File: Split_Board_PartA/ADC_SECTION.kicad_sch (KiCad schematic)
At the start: 58 parts, among them J2 Conn_01x28, U26 MCP604, U27 MCP604, U28 ADC128S102CIMTX_NOPB

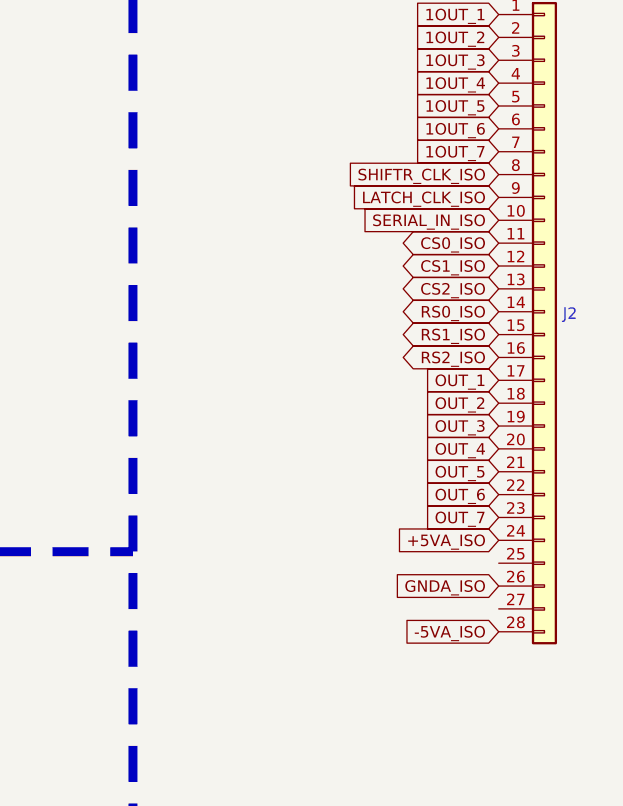
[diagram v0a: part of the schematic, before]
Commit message: added led pins in part A of slave boards
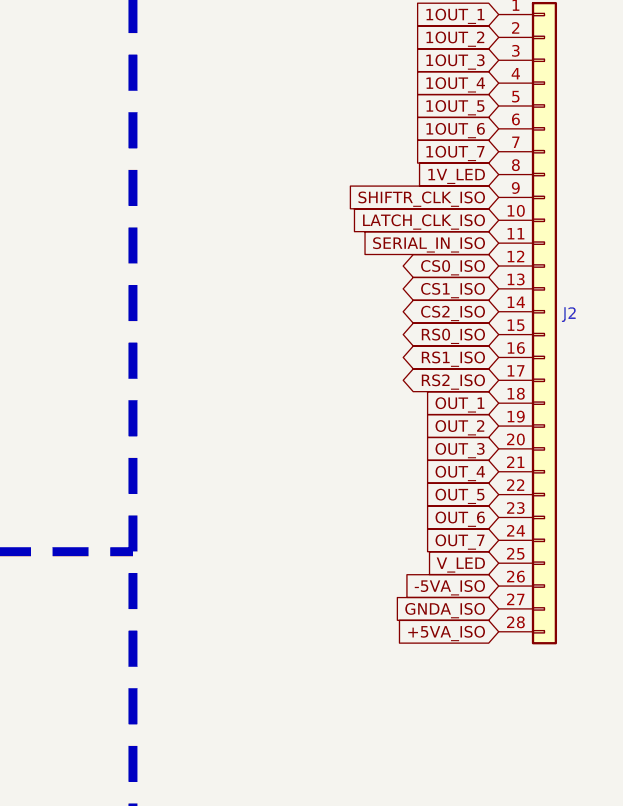
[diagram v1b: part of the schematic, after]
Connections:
- net +5VA_ISO: now also J2.28 (Pin_28); no longer J2.24 (Pin_24)
- net -5VA_ISO: now also J2.26 (Pin_26); no longer J2.28 (Pin_28)
- net CS0_ISO: now also J2.12 (Pin_12); no longer J2.11 (Pin_11)
- net CS1_ISO: now also J2.13 (Pin_13); no longer J2.12 (Pin_12)
- net CS2_ISO: now also J2.14 (Pin_14); no longer J2.13 (Pin_13)
- net GNDA_ISO: now also J2.27 (Pin_27); no longer J2.26 (Pin_26)
- net LATCH_CLK_ISO: now also J2.10 (Pin_10); no longer J2.9 (Pin_9)
- net OUT_1: now also J2.18 (Pin_18); no longer J2.17 (Pin_17)
- net OUT_2: now also J2.19 (Pin_19); no longer J2.18 (Pin_18)
- net OUT_3: now also J2.20 (Pin_20); no longer J2.19 (Pin_19)
- net OUT_4: now also J2.21 (Pin_21); no longer J2.20 (Pin_20)
- net OUT_5: now also J2.22 (Pin_22); no longer J2.21 (Pin_21)
- net OUT_6: now also J2.23 (Pin_23); no longer J2.22 (Pin_22)
- net OUT_7: now also J2.24 (Pin_24); no longer J2.23 (Pin_23)
- net RS0_ISO: now also J2.15 (Pin_15); no longer J2.14 (Pin_14)
- net RS1_ISO: now also J2.16 (Pin_16); no longer J2.15 (Pin_15)
- net RS2_ISO: now also J2.17 (Pin_17); no longer J2.16 (Pin_16)
- net SERIAL_IN_ISO: now also J2.11 (Pin_11); no longer J2.10 (Pin_10)
- net SHIFTR_CLK_ISO: now also J2.9 (Pin_9); no longer J2.8 (Pin_8)
- net V_LED: now reaches J2.25 (Pin_25)
- new net 1V_LED: J2.8 (Pin_8)

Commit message: Removed the gerber files of espv5.0
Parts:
- R61, R62, R63, R64, R67, R68, R71, R72: value 100E -> 0E
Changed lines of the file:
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@@
       (effects (font (size 1.27 1.27)) (justify right))
     )
-    (property "Value" "100E" (at 100.457 60.1472 0)
+    (property "Value" "0E" (at 100.457 60.1472 0)
       (effects (font (size 1.27 1.27)) (justify right))
     )
@@
       (effects (font (size 1.27 1.27)) (justify right))
     )
-    (property "Value" "100E" (at 49.657 190.3222 0)
+    (property "Value" "0E" (at 49.657 190.3222 0)
       (effects (font (size 1.27 1.27)) (justify right))
     )
@@
       (effects (font (size 1.27 1.27)) (justify right))
     )
-    (property "Value" "100E" (at 100.457 190.3222 0)
+    (property "Value" "0E" (at 100.457 190.3222 0)
       (effects (font (size 1.27 1.27)) (justify right))
     )
@@
       (effects (font (size 1.27 1.27)) (justify right))
     )
-    (property "Value" "100E" (at 49.657 215.7222 0)
+    (property "Value" "0E" (at 49.657 215.7222 0)
       (effects (font (size 1.27 1.27)) (justify right))
     )
@@
       (effects (font (size 1.27 1.27)) (justify right))
     )
-    (property "Value" "100E" (at 49.657 85.5472 0)
+    (property "Value" "0E" (at 49.657 85.5472 0)
       (effects (font (size 1.27 1.27)) (justify right))
     )
@@
       (effects (font (size 1.27 1.27)) (justify right))
     )
-    (property "Value" "100E" (at 100.457 85.5472 0)
+    (property "Value" "0E" (at 100.457 85.5472 0)
       (effects (font (size 1.27 1.27)) (justify right))
     )
@@
       (effects (font (size 1.27 1.27)) (justify right))
     )
-    (property "Value" "100E" (at 50.292 110.9472 0)
+    (property "Value" "0E" (at 50.292 110.9472 0)
       (effects (font (size 1.27 1.27)) (justify right))
     )
@@
       (effects (font (size 1.27 1.27)) (justify right))
     )
-    (property "Value" "100E" (at 100.457 241.1222 0)
+    (property "Value" "0E" (at 100.457 241.1222 0)
       (effects (font (size 1.27 1.27)) (justify right))
     )
@@
       (effects (font (size 1.27 1.27)) (justify right))
     )
-    (property "Value" "100E" (at 49.657 60.1472 0)
+    (property "Value" "0E" (at 49.657 60.1472 0)
       (effects (font (size 1.27 1.27)) (justify right))
     )
@@
       (effects (font (size 1.27 1.27)) (justify right))
     )
-    (property "Value" "100E" (at 100.457 110.9472 0)
+    (property "Value" "0E" (at 100.457 110.9472 0)
       (effects (font (size 1.27 1.27)) (justify right))
     )
@@
       (effects (font (size 1.27 1.27)) (justify right))
     )
-    (property "Value" "100E" (at 101.092 168.0972 0)
+    (property "Value" "0E" (at 101.092 168.0972 0)
       (effects (font (size 1.27 1.27)) (justify right))
     )
@@
       (effects (font (size 1.27 1.27)) (justify right))
     )
-    (property "Value" "100E" (at 47.752 37.9222 0)
+    (property "Value" "0E" (at 47.752 37.9222 0)
       (effects (font (size 1.27 1.27)) (justify right))
     )
@@
       (effects (font (size 1.27 1.27)) (justify right))
     )
-    (property "Value" "100E" (at 101.092 37.9222 0)
+    (property "Value" "0E" (at 101.092 37.9222 0)
       (effects (font (size 1.27 1.27)) (justify right))
     )
@@
       (effects (font (size 1.27 1.27)) (justify right))
     )
-    (property "Value" "100E" (at 100.457 215.7222 0)
+    (property "Value" "0E" (at 100.457 215.7222 0)
       (effects (font (size 1.27 1.27)) (justify right))
     )
@@
       (effects (font (size 1.27 1.27)) (justify right))
     )
-    (property "Value" "100E" (at 47.752 168.0972 0)
+    (property "Value" "0E" (at 47.752 168.0972 0)
       (effects (font (size 1.27 1.27)) (justify right))
     )
@@
       (effects (font (size 1.27 1.27)) (justify right))
     )
-    (property "Value" "100E" (at 50.292 241.1222 0)
+    (property "Value" "0E" (at 50.292 241.1222 0)
       (effects (font (size 1.27 1.27)) (justify right))
     )

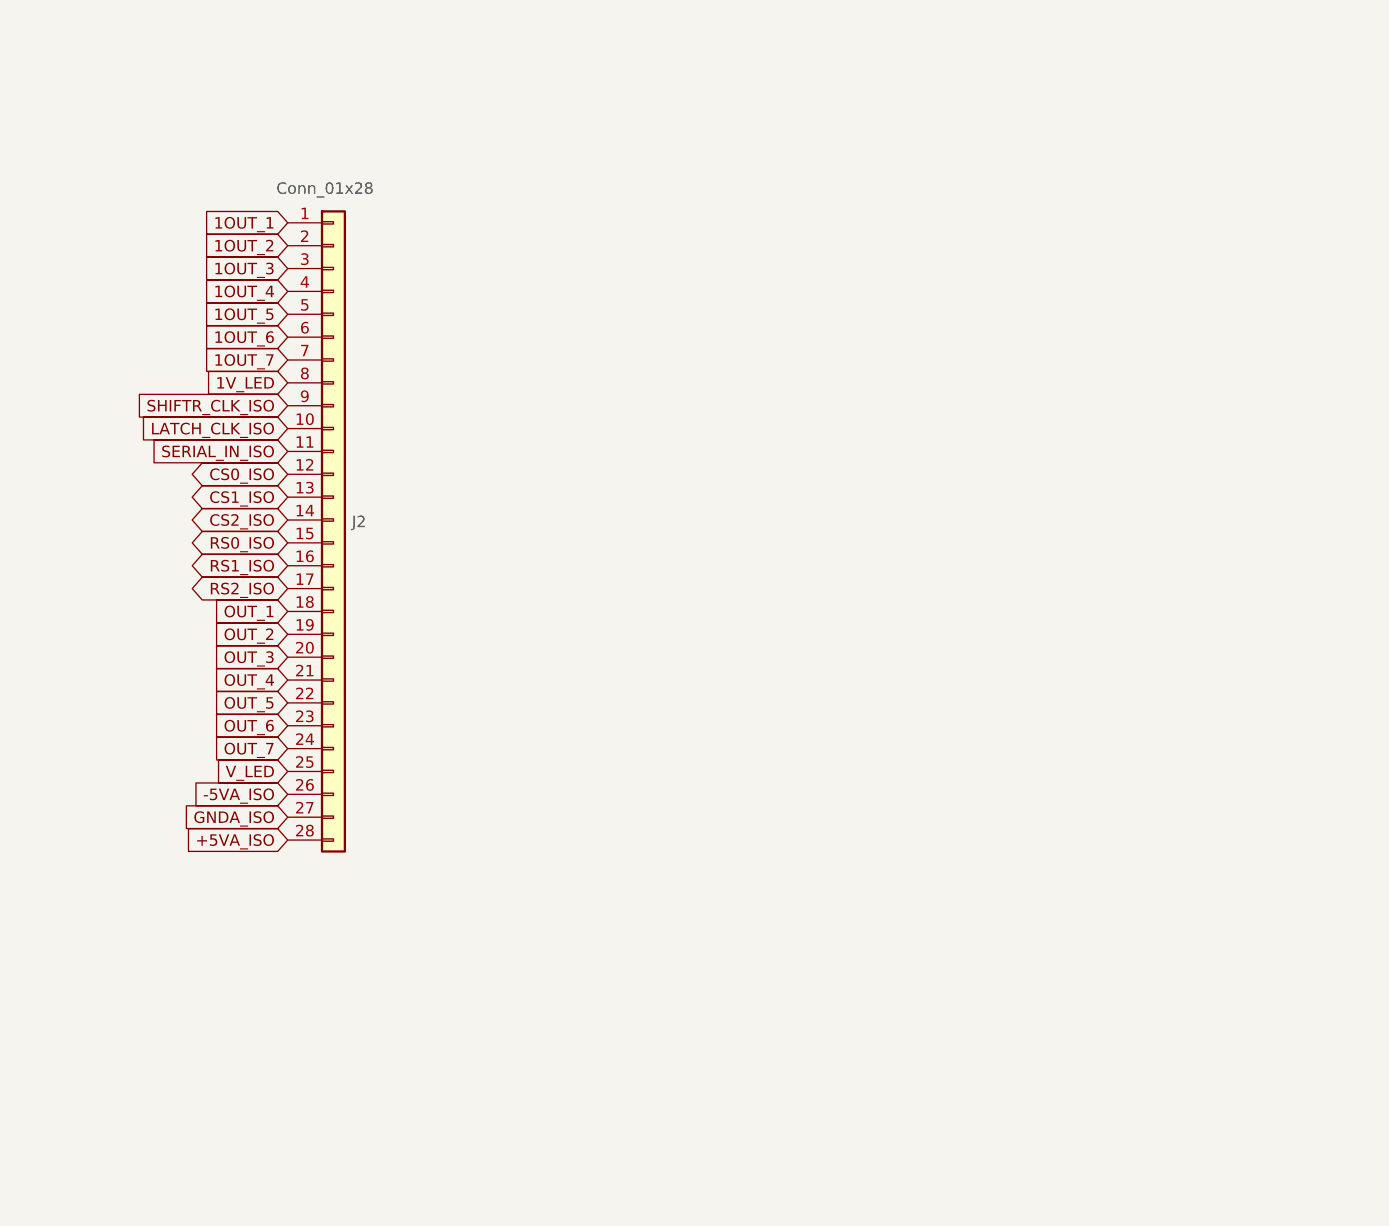
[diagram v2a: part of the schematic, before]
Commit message: added a adapter board in part b and edited the db37 connector in part A
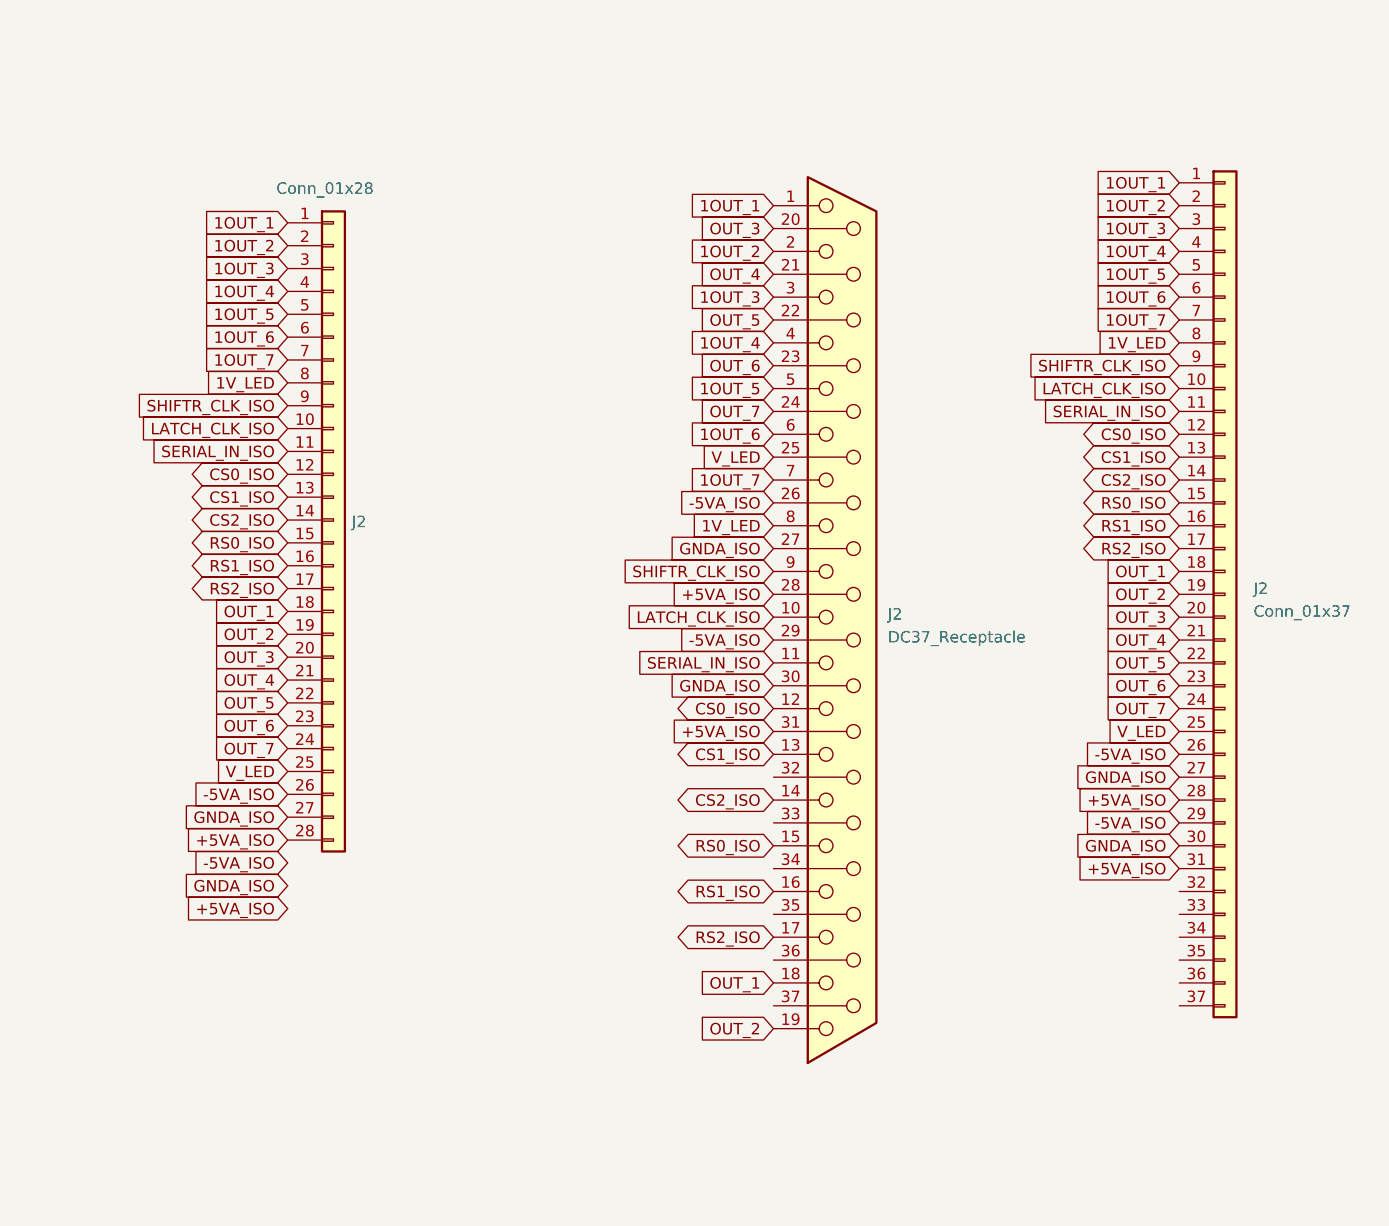
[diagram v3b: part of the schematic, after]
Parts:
- added J2: Conn_01x37, symbol Connector_Generic:Conn_01x37
- added J2: DC37_Receptacle, symbol Connector:DC37_Receptacle
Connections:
- net +5VA_ISO: now also J2.28, J2.28 (Pin_28), J2.31, J2.31 (Pin_31)
- net -5VA_ISO: now also J2.26, J2.26 (Pin_26), J2.29, J2.29 (Pin_29)
- net 1OUT_1: now also J2.1, J2.1 (Pin_1)
- net 1OUT_2: now also J2.2, J2.2 (Pin_2)
- net 1OUT_3: now also J2.3, J2.3 (Pin_3)
- net 1OUT_4: now also J2.4, J2.4 (Pin_4)
- net 1OUT_5: now also J2.5, J2.5 (Pin_5)
- net 1OUT_6: now also J2.6, J2.6 (Pin_6)
- net 1OUT_7: now also J2.7, J2.7 (Pin_7)
- net 1V_LED: now also J2.8, J2.8 (Pin_8)
- net CS0_ISO: now also J2.12, J2.12 (Pin_12)
- net CS1_ISO: now also J2.13, J2.13 (Pin_13)
- net CS2_ISO: now also J2.14, J2.14 (Pin_14)
- net GNDA_ISO: now also J2.27, J2.27 (Pin_27), J2.30, J2.30 (Pin_30)
- net LATCH_CLK_ISO: now also J2.10, J2.10 (Pin_10)
- net OUT_1: now also J2.18, J2.18 (Pin_18)
- net OUT_2: now also J2.19, J2.19 (Pin_19)
- net OUT_3: now also J2.20, J2.20 (Pin_20)
- net OUT_4: now also J2.21, J2.21 (Pin_21)
- net OUT_5: now also J2.22, J2.22 (Pin_22)
- net OUT_6: now also J2.23, J2.23 (Pin_23)
- net OUT_7: now also J2.24, J2.24 (Pin_24)
- net RS0_ISO: now also J2.15, J2.15 (Pin_15)
- net RS1_ISO: now also J2.16, J2.16 (Pin_16)
- net RS2_ISO: now also J2.17, J2.17 (Pin_17)
- net SERIAL_IN_ISO: now also J2.11, J2.11 (Pin_11)
- net SHIFTR_CLK_ISO: now also J2.9, J2.9 (Pin_9)
- net V_LED: now also J2.25, J2.25 (Pin_25)
